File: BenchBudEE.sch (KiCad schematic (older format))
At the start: 0 parts

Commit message: Hooked up top level schematic
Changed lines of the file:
@@
 $EndDescr
 $Sheet
-S 2200 4750 1650 2350
-U 52ED1A8D
-F0 "Arduino" 50
-F1 "Arduino.sch" 50
-F2 "Relay+" O R 3850 6750 60
-F3 "Relay-" I R 3850 6900 60
-F4 "MOSI" O R 3850 6100 60
-F5 "MISO" I R 3850 6200 60
-F6 "SCLK" O R 3850 6300 60
-F7 "CS_N" O R 3850 6400 60
-F8 "LED_EN" O R 3850 5550 60
-F9 "LED_FREQ" O R 3850 5700 60
-$EndSheet
-$Sheet
-S 7250 5450 1500 700
+S 7250 4250 1500 700
 U 52ED1AE1
 F0 "ThermoCouple" 50
 F1 "ThermoCouple.sch" 50
-F2 "TC IN +" I R 8750 5650 60
-F3 "TC IN -" I R 8750 5850 60
-F4 "MOSI" I L 7250 5600 60
-F5 "MISO" O L 7250 5750 60
-F6 "SCLK" I L 7250 5900 60
-F7 "CS_N" I L 7250 6050 60
-$EndSheet
-$Sheet
-S 7300 6450 1450 450
+F2 "TC IN +" I R 8750 4450 60
+F3 "TC IN -" I R 8750 4650 60
+F4 "MOSI" I L 7250 4400 60
+F5 "MISO" O L 7250 4550 60
+F6 "SCLK" I L 7250 4700 60
+F7 "CS_N" I L 7250 4850 60
+$EndSheet
+$Sheet
+S 7300 6450 1450 600
 U 52ED1B00
 F0 "Relay" 50
 F1 "Relay.sch" 50
-F2 "DIN+" I L 7300 6600 60
-F3 "DIN-" O L 7300 6750 60
-F4 "Relay+" I R 8750 6600 60
-F5 "Relay-" O R 8750 6750 60
+F2 "RELAY_NO" B R 8750 6600 60
+F3 "RELAY_NC" B R 8750 6750 60
+F4 "RELAY_COM" B R 8750 6900 60
+F5 "RELAY+" I L 7300 6600 60
+F6 "RELAY-" O L 7300 6750 60
 $EndSheet
 $Sheet
@@
 $EndSheet
 $Sheet
-S 7250 4500 1400 600
+S 7250 5450 1400 600
 U 52ED1B6A
 F0 "LED_Driver" 50
 F1 "LED_Driver.sch" 50
-F2 "EN" I L 7250 4700 60
-F3 "FREQ" I L 7250 4900 60
-F4 "String+" O R 8650 4700 60
-F5 "String-" I R 8650 4900 60
+F2 "FREQ" I L 7250 5850 60
+F3 "LED_EN_PWM" I L 7250 5650 60
+F4 "LED_STRING+" O R 8650 5650 60
+F5 "LED_STRING-" O R 8650 5850 60
 $EndSheet
 $Sheet
@@
 F0 "Fan" 50
 F1 "Fan.sch" 50
-F2 "Power+" O R 8600 2850 60
-F3 "Power-" I R 8600 3050 60
-F4 "Tach" I R 8600 3250 60
-F5 "Tach_Out" O L 7250 3200 60
-F6 "Fan_In" I L 7250 3050 60
-F7 "MOSI" I L 7250 3550 60
-F8 "MISO" O L 7250 3650 60
-F9 "SCLK" I L 7250 3750 60
-F10 "CS_N" I L 7250 3850 60
-F11 "Current Measure" O L 7250 3350 60
-$EndSheet
-$Sheet
-S 9950 1100 650  5650
+F2 "MOSI" I L 7250 3550 60
+F3 "MISO" O L 7250 3650 60
+F4 "SCLK" I L 7250 3750 60
+F5 "CS_N" I L 7250 3850 60
+F6 "FAN_OUT+" O R 8600 2850 60
+F7 "TACH_IN" I R 8600 3250 60
+F8 "TACH_MEAS" O L 7250 2800 60
+F9 "FAN_EN_N" I L 7250 3400 60
+F10 "CURR_MEAS" O L 7250 2950 60
+F11 "FAN_OUT-" O R 8600 3000 60
+$EndSheet
+$Sheet
+S 9950 1100 1100 5800
 U 52ED1C0B
 F0 "TerminalBlock" 50
 F1 "TerminalBlock.sch" 50
+F2 "V+_ADJ" I L 9950 1450 60
+F3 "V-_ADJ" I L 9950 1600 60
+F4 "FAN_OUT+" I L 9950 2850 60
+F5 "FAN_OUT-" I L 9950 3000 60
+F6 "TACH_IN" O L 9950 3250 60
+F7 "LED_STRING+" O L 9950 5600 60
+F8 "LED_STRING-" O L 9950 5800 60
+F9 "TC_IN+" O L 9950 4450 60
+F10 "TC_IN-" O L 9950 4650 60
+F11 "RELAY_NO" B L 9950 6300 60
+F12 "RELAY_NC" B L 9950 6450 60
+F13 "RELAY_COM" B L 9950 6600 60
 $EndSheet
 $Sheet
@@
 F9 "V-_CURR_MON" O L 7250 2100 60
 $EndSheet
+Wire Wire Line
+	9950 1450 8850 1450
+Wire Wire Line
+	8850 1600 9950 1600
+Wire Wire Line
+	9950 2850 8600 2850
+Wire Wire Line
+	8600 3000 9950 3000
+Wire Wire Line
+	9950 3250 8600 3250
+Wire Wire Line
+	8750 6600 9200 6600
+Wire Wire Line
+	9200 6600 9200 6300
+Wire Wire Line
+	9200 6300 9950 6300
+Wire Wire Line
+	8750 6750 9250 6750
+Wire Wire Line
+	9250 6750 9250 6450
+Wire Wire Line
+	9250 6450 9950 6450
+Wire Wire Line
+	8750 6900 9300 6900
+Wire Wire Line
+	9300 6900 9300 6600
+Wire Wire Line
+	9300 6600 9950 6600
+Wire Wire Line
+	3350 4250 5150 4250
+Wire Wire Line
+	5150 4250 5150 1650
+Wire Wire Line
+	5150 1650 7250 1650
+Wire Wire Line
+	3350 4400 5300 4400
+Wire Wire Line
+	5300 4400 5300 1800
+Wire Wire Line
+	5300 1800 7250 1800
+Wire Wire Line
+	5800 3400 7250 3400
+Wire Wire Line
+	5800 3400 5800 4700
+Wire Wire Line
+	5800 4700 3350 4700
+$Sheet
+S 1700 4100 1650 3050
+U 52ED1A8D
+F0 "Arduino" 50
+F1 "Arduino.sch" 50
+F2 "MOSI" O R 3350 4850 60
+F3 "MISO" I R 3350 4950 60
+F4 "SCLK" O R 3350 5050 60
+F5 "LED_FREQ" O R 3350 5900 60
+F6 "Fan_En_N" O R 3350 4700 60
+F7 "Tach_Meas" I R 3350 5600 60
+F8 "CURR_MEAS" I R 3350 5450 60
+F9 "RELAY+" O R 3350 6700 60
+F10 "RELAY-" I R 3350 6850 60
+F11 "LED_EN_PWM" O R 3350 5750 60
+F12 "V+_ADJ_MON" I R 3350 4250 60
+F13 "V-_ADJ_MON" I R 3350 4400 60
+F14 "DAC_CS_N" O R 3350 5150 60
+F15 "ADC_CS_N" O R 3350 5300 60
+$EndSheet
+Wire Wire Line
+	7250 3550 5900 3550
+Wire Wire Line
+	5900 3550 5900 4850
+Wire Wire Line
+	5900 4850 3350 4850
+Wire Wire Line
+	3350 4950 6000 4950
+Wire Wire Line
+	6000 4950 6000 3650
+Wire Wire Line
+	6000 3650 7250 3650
+Wire Wire Line
+	7250 3750 6100 3750
+Wire Wire Line
+	6100 3750 6100 5050
+Wire Wire Line
+	6100 5050 3350 5050
+Wire Wire Line
+	3350 5150 6200 5150
+Wire Wire Line
+	6200 5150 6200 3850
+Wire Wire Line
+	6200 3850 7250 3850
+Wire Wire Line
+	7250 4850 6700 4850
+Wire Wire Line
+	6700 4850 6700 5300
+Wire Wire Line
+	6700 5300 3350 5300
+Wire Wire Line
+	7250 4700 6100 4700
+Connection ~ 6100 4700
+Wire Wire Line
+	6000 4550 7250 4550
+Connection ~ 6000 4550
+Wire Wire Line
+	7250 4400 5900 4400
+Connection ~ 5900 4400
+Wire Wire Line
+	7250 2950 5600 2950
+Wire Wire Line
+	5600 2950 5600 5450
+Wire Wire Line
+	5600 5450 3350 5450
+Wire Wire Line
+	3350 5600 5500 5600
+Wire Wire Line
+	5500 5600 5500 2800
+Wire Wire Line
+	5500 2800 7250 2800
+Wire Wire Line
+	8750 4450 9950 4450
+Wire Wire Line
+	8750 4650 9950 4650
+Wire Wire Line
+	8650 5650 9500 5650
+Wire Wire Line
+	9500 5650 9500 5600
+Wire Wire Line
+	9500 5600 9950 5600
+Wire Wire Line
+	8650 5850 9600 5850
+Wire Wire Line
+	9600 5850 9600 5800
+Wire Wire Line
+	9600 5800 9950 5800
 $EndSCHEMATC

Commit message: Fan Current module refactoring
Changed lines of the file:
@@
 F0 "LED_Driver" 50
 F1 "LED_Driver.sch" 50
-F2 "FREQ" I L 7250 5850 60
 F3 "LED_EN_PWM" I L 7250 5650 60
 F4 "LED_STRING+" O R 8650 5650 60
@@
 F7 "TACH_IN" I R 8600 3250 60
 F8 "TACH_MEAS" O L 7250 2800 60
-F9 "FAN_EN_N" I L 7250 3400 60
-F10 "CURR_MEAS" O L 7250 2950 60
-F11 "FAN_OUT-" O R 8600 3000 60
+F9 "CURR_MEAS" O L 7250 2950 60
+F10 "FAN_OUT-" O R 8600 3000 60
+F11 "FAN_PWM" I L 7250 3400 60
+F12 "FAN_MODE" I L 7250 3150 60
 $EndSheet
 $Sheet
@@
 F3 "MISO" I R 3350 4950 60
 F4 "SCLK" O R 3350 5050 60
-F5 "LED_FREQ" O R 3350 5900 60
-F6 "Fan_En_N" O R 3350 4700 60
-F7 "Tach_Meas" I R 3350 5600 60
-F8 "CURR_MEAS" I R 3350 5450 60
-F9 "RELAY+" O R 3350 6700 60
-F10 "RELAY-" I R 3350 6850 60
-F11 "LED_EN_PWM" O R 3350 5750 60
-F12 "V+_ADJ_MON" I R 3350 4250 60
-F13 "V-_ADJ_MON" I R 3350 4400 60
-F14 "DAC_CS_N" O R 3350 5150 60
-F15 "ADC_CS_N" O R 3350 5300 60
+F5 "Tach_Meas" I R 3350 5600 60
+F6 "CURR_MEAS" I R 3350 5450 60
+F7 "RELAY+" O R 3350 6700 60
+F8 "RELAY-" I R 3350 6850 60
+F9 "LED_EN_PWM" O R 3350 5750 60
+F10 "V+_ADJ_MON" I R 3350 4250 60
+F11 "V-_ADJ_MON" I R 3350 4400 60
+F12 "DAC_CS_N" O R 3350 5150 60
+F13 "ADC_CS_N" O R 3350 5300 60
+F14 "Fan_PWM" O R 3350 4700 60
+F15 "FAN_MODE" O R 3350 4550 60
 $EndSheet
 Wire Wire Line
@@
 Wire Wire Line
 	9600 5800 9950 5800
+Wire Wire Line
+	6500 6700 6500 6600
+Wire Wire Line
+	6500 6600 7300 6600
+Wire Wire Line
+	3350 6700 6500 6700
+Wire Wire Line
+	3350 6850 6950 6850
+Wire Wire Line
+	6950 6850 6950 6750
+Wire Wire Line
+	6950 6750 7300 6750
+Wire Wire Line
+	3350 5750 6850 5750
+Wire Wire Line
+	6850 5750 6850 5650
+Wire Wire Line
+	6850 5650 7250 5650
+Wire Wire Line
+	7250 3150 5700 3150
+Wire Wire Line
+	5700 3150 5700 4550
+Wire Wire Line
+	5700 4550 3350 4550
 $EndSCHEMATC

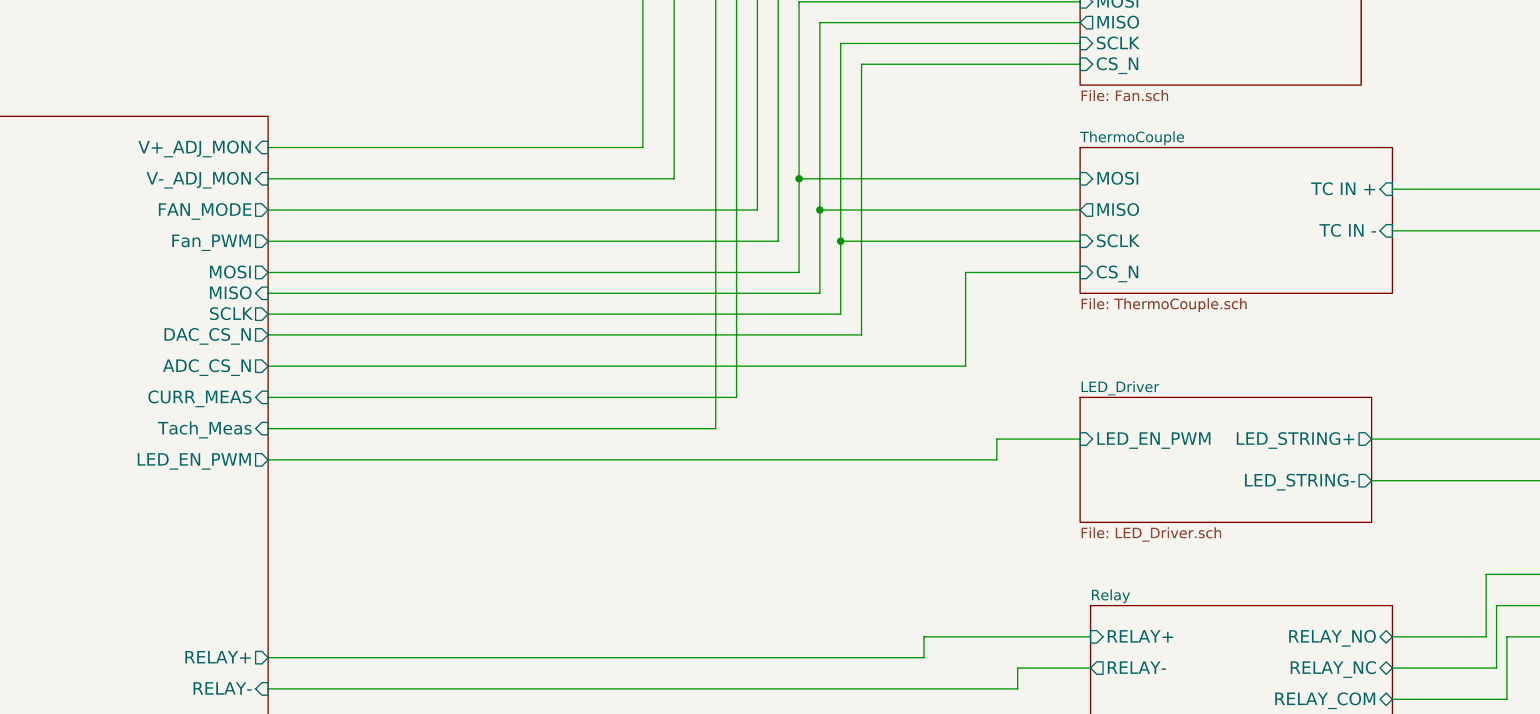
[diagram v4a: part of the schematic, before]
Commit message: Associated Thermocouple module
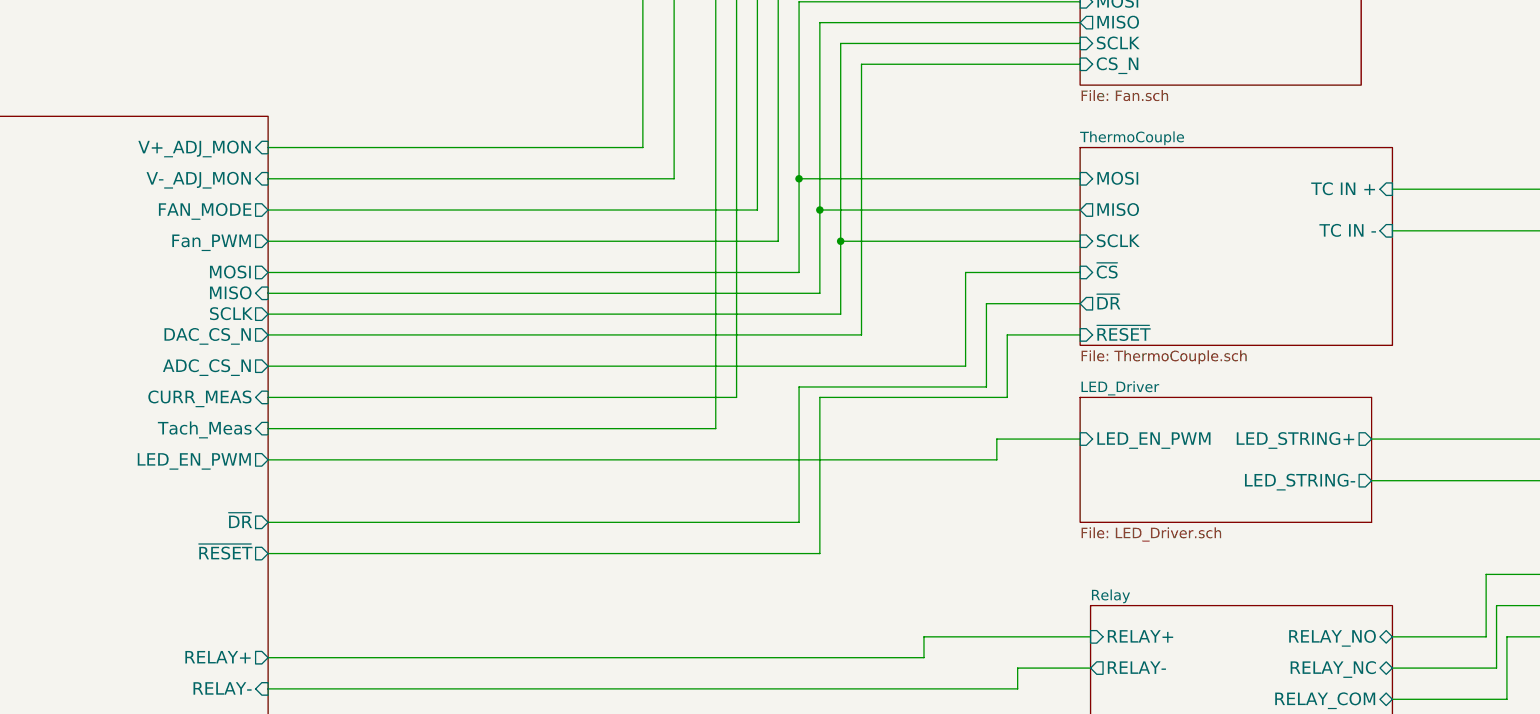
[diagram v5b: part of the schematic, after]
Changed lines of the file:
@@
 $EndDescr
 $Sheet
-S 7250 4250 1500 700
+S 7250 4250 1500 950
 U 52ED1AE1
 F0 "ThermoCouple" 50
@@
 F5 "MISO" O L 7250 4550 60
 F6 "SCLK" I L 7250 4700 60
-F7 "CS_N" I L 7250 4850 60
+F7 "~CS" I L 7250 4850 60
+F8 "~DR" O L 7250 5000 60
+F9 "~RESET" I L 7250 5150 60
 $EndSheet
 $Sheet
@@
 F14 "Fan_PWM" O R 3350 4700 60
 F15 "FAN_MODE" O R 3350 4550 60
+F16 "~DR" O R 3350 6050 60
+F17 "~RESET" O R 3350 6200 60
 $EndSheet
 Wire Wire Line
@@
 Wire Wire Line
 	5700 4550 3350 4550
+Wire Wire Line
+	7250 5000 6800 5000
+Wire Wire Line
+	6800 5000 6800 5400
+Wire Wire Line
+	6800 5400 5900 5400
+Wire Wire Line
+	5900 5400 5900 6050
+Wire Wire Line
+	5900 6050 3350 6050
+Wire Wire Line
+	7250 5150 6900 5150
+Wire Wire Line
+	6900 5150 6900 5450
+Wire Wire Line
+	6900 5450 6000 5450
+Wire Wire Line
+	6000 5450 6000 6200
+Wire Wire Line
+	6000 6200 3350 6200
 $EndSCHEMATC

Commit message: more changes?
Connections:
- wire segments 77 -> 82
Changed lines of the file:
@@
 $EndSheet
 $Sheet
-S 7250 2700 1350 1250
+S 7250 2700 1500 1400
 U 52ED1BE8
 F0 "Fan" 50
 F1 "Fan.sch" 50
-F2 "MOSI" I L 7250 3550 60
-F3 "MISO" O L 7250 3650 60
-F4 "SCLK" I L 7250 3750 60
-F5 "CS_N" I L 7250 3850 60
-F6 "FAN_OUT+" O R 8600 2850 60
-F7 "TACH_IN" I R 8600 3250 60
-F8 "TACH_MEAS" O L 7250 2800 60
-F9 "CURR_MEAS" O L 7250 2950 60
-F10 "FAN_OUT-" O R 8600 3000 60
-F11 "FAN_PWM" I L 7250 3400 60
-F12 "FAN_MODE" I L 7250 3150 60
+F2 "MOSI" I L 7250 3400 60
+F3 "SCLK" I L 7250 3550 60
+F4 "CS_N" I L 7250 3700 60
+F5 "FAN_OUT+" O R 8750 2850 60
+F6 "TACH_IN" I R 8750 3250 60
+F7 "TACH_MEAS" O L 7250 2800 60
+F8 "CURR_MEAS" O L 7250 2950 60
+F9 "FAN_OUT-" O R 8750 3000 60
+F10 "FAN_PWM" I L 7250 3250 60
+F11 "FAN_MODE" I L 7250 3100 60
+F12 "~LDAC" I L 7250 3850 60
+F13 "~SHDN" I L 7250 4000 60
 $EndSheet
 $Sheet
@@
 	5300 1800 7250 1800
 Wire Wire Line
-	5800 3400 7250 3400
-Wire Wire Line
-	5800 3400 5800 4700
+	5800 3250 7250 3250
+Wire Wire Line
+	5800 3250 5800 4700
 Wire Wire Line
 	5800 4700 3350 4700
@@
 F10 "V+_ADJ_MON" I R 3350 4250 60
 F11 "V-_ADJ_MON" I R 3350 4400 60
-F12 "DAC_CS_N" O R 3350 5150 60
-F13 "ADC_CS_N" O R 3350 5300 60
-F14 "Fan_PWM" O R 3350 4700 60
-F15 "FAN_MODE" O R 3350 4550 60
-F16 "~DR" O R 3350 6050 60
-F17 "~RESET" O R 3350 6200 60
-$EndSheet
-Wire Wire Line
-	7250 3550 5900 3550
-Wire Wire Line
-	5900 3550 5900 4850
+F12 "Fan_PWM" O R 3350 4700 60
+F13 "FAN_MODE" O R 3350 4550 60
+F14 "~DR" O R 3350 6050 60
+F15 "~RESET" O R 3350 6200 60
+F16 "~LDAC" I R 3350 6400 60
+F17 "~SHDN" O R 3350 6550 60
+F18 "~ADC_CS" O R 3350 5300 60
+F19 "~DAC_CS" O R 3350 5150 60
+$EndSheet
+Wire Wire Line
+	7250 3400 5900 3400
+Wire Wire Line
+	5900 3400 5900 4850
 Wire Wire Line
 	5900 4850 3350 4850
@@
 	3350 4950 6000 4950
 Wire Wire Line
-	6000 4950 6000 3650
-Wire Wire Line
-	6000 3650 7250 3650
-Wire Wire Line
-	7250 3750 6100 3750
-Wire Wire Line
-	6100 3750 6100 5050
+	7250 3550 6100 3550
+Wire Wire Line
+	6100 3550 6100 5050
 Wire Wire Line
 	6100 5050 3350 5050
@@
 	3350 5150 6200 5150
 Wire Wire Line
-	6200 5150 6200 3850
-Wire Wire Line
-	6200 3850 7250 3850
+	6200 5150 6200 3700
+Wire Wire Line
+	6200 3700 7250 3700
 Wire Wire Line
 	7250 4850 6700 4850
@@
 	6850 5650 7250 5650
 Wire Wire Line
-	7250 3150 5700 3150
-Wire Wire Line
-	5700 3150 5700 4550
+	7250 3100 5700 3100
+Wire Wire Line
+	5700 3100 5700 4550
 Wire Wire Line
 	5700 4550 3350 4550
@@
 Wire Wire Line
 	6000 6200 3350 6200
+Wire Wire Line
+	6000 4950 6000 4550
+Wire Wire Line
+	7250 3850 6300 3850
+Wire Wire Line
+	6300 3850 6300 6400
+Wire Wire Line
+	6300 6400 3350 6400
+Wire Wire Line
+	7250 4000 6400 4000
+Wire Wire Line
+	6400 4000 6400 6550
+Wire Wire Line
+	6400 6550 3350 6550
 $EndSCHEMATC
